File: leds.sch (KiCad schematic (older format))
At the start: 40 parts, among them SW1 SW_PUSH-MX_W_LED, SW10 SW_PUSH-MX_W_LED, SW11 SW_PUSH-MX_W_LED, SW12 SW_PUSH-MX_W_LED, SW13 SW_PUSH-MX_W_LED, SW14 SW_PUSH-MX_W_LED, SW15 SW_PUSH-MX_W_LED, SW16 SW_PUSH-MX_W_LED, SW17 SW_PUSH-MX_W_LED, SW18 SW_PUSH-MX_W_LED, SW19 SW_PUSH-MX_W_LED, SW2 SW_PUSH-MX_W_LED, SW20 SW_PUSH-MX_W_LED, SW3 SW_PUSH-MX_W_LED, SW4 SW_PUSH-MX_W_LED, SW5 SW_PUSH-MX_W_LED, SW6 SW_PUSH-MX_W_LED, SW7 SW_PUSH-MX_W_LED, SW8 SW_PUSH-MX_W_LED, SW9 SW_PUSH-MX_W_LED

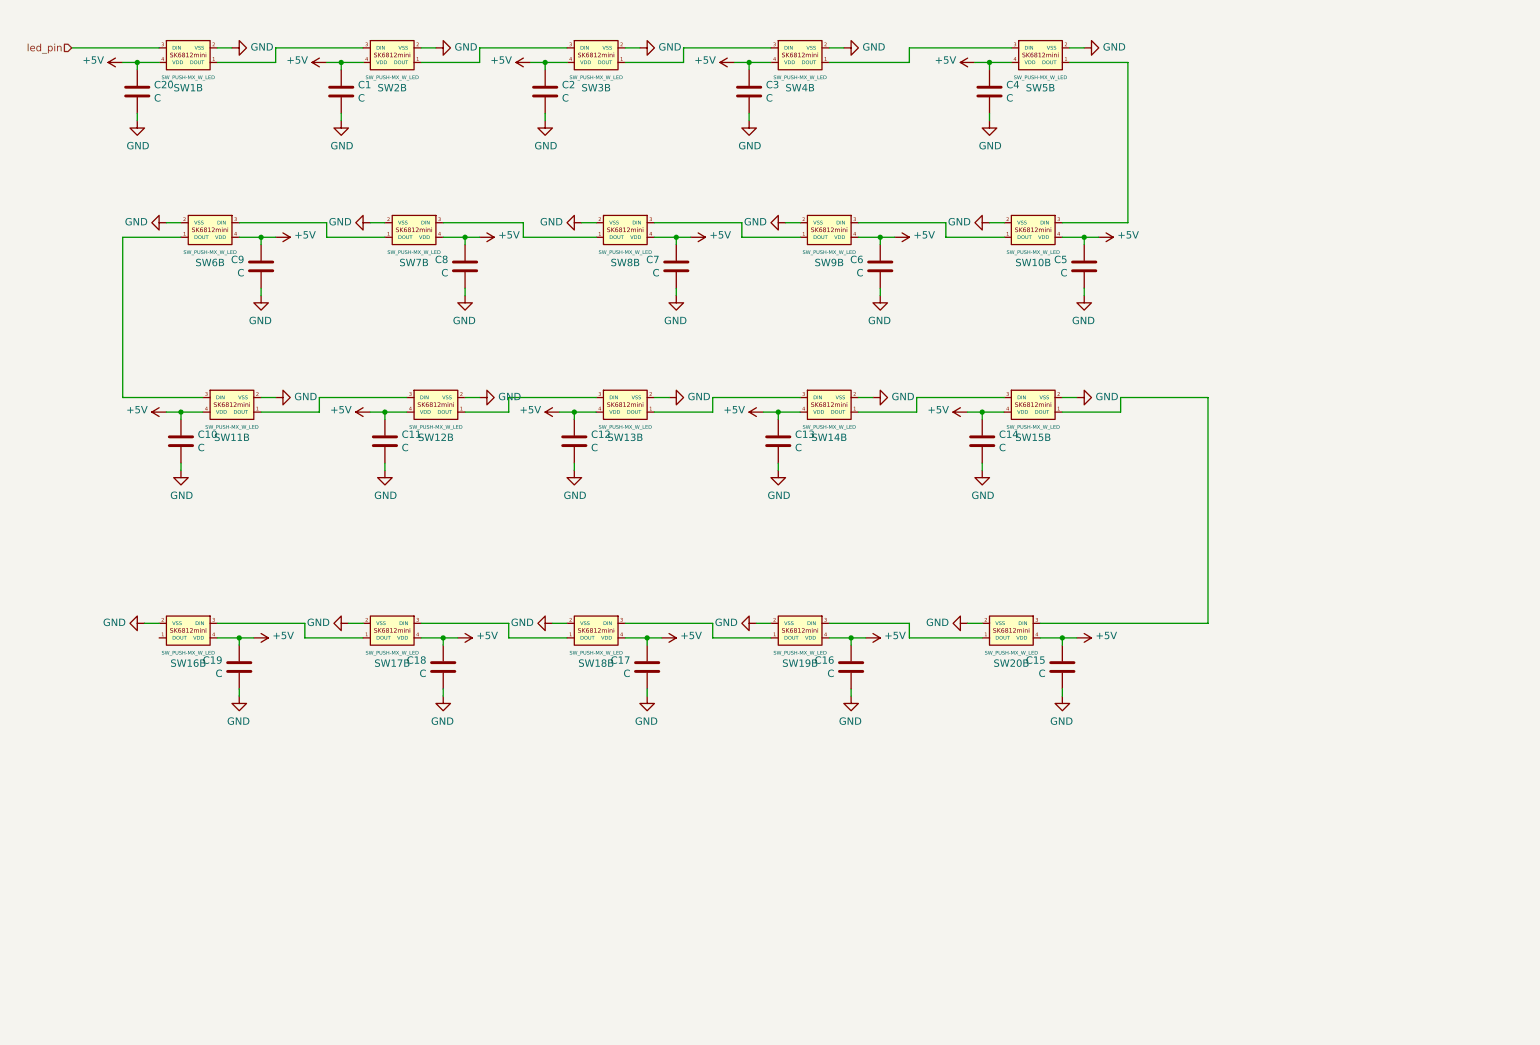
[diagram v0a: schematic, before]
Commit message: kinda done, about to add jumpers for rot. enc.
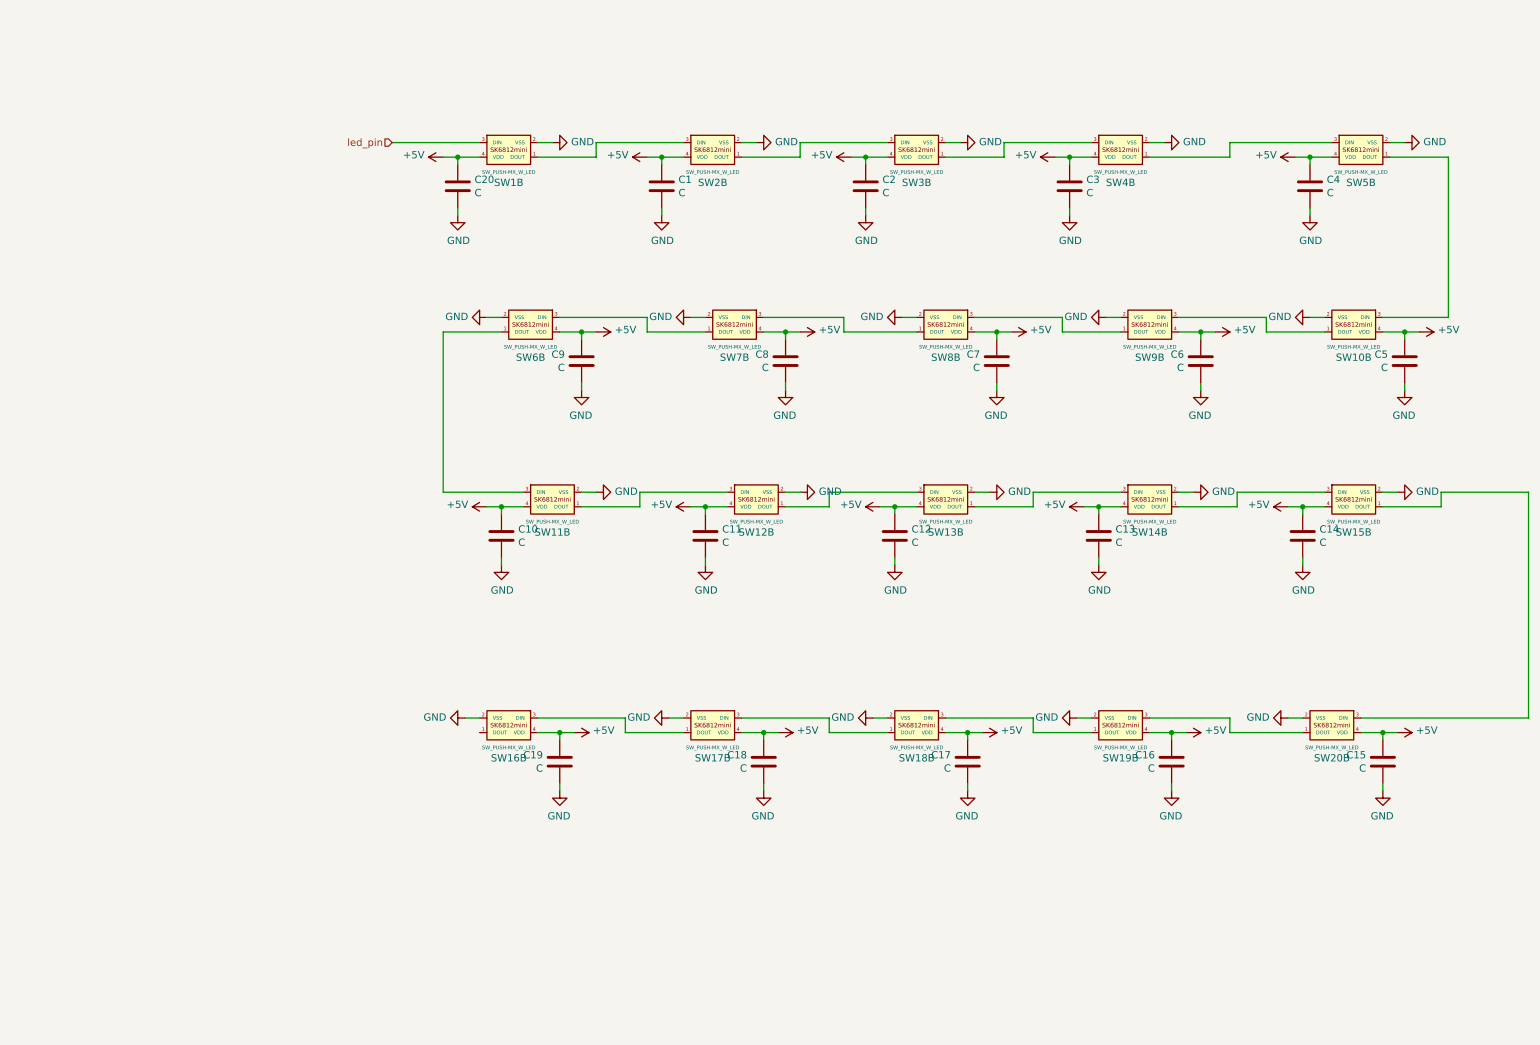
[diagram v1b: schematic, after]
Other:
- moved on the sheet: C1, C10, C11, C12, C13, C14, C15, C16, C17, C18, C19, C2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

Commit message: about to add underglow
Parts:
- added C21, C22, C23, C24: C, Capacitor_SMD:C_0805_2012Metric_Pad1.18x1.45mm_HandSolder, symbol Device:C
- added JP1: Jumper_2_Open, Jumper:SolderJumper-2_P1.3mm_Open_TrianglePad1.0x1.5mm, symbol Jumper:Jumper_2_Open
- added SW23, SW24, SW25, SW26: SW_PUSH-MX_W_LED, sofle RGB:SK6812MINI_and_cherry_oneside_ledflipped, symbol sofle_rgb:SW_PUSH-MX_W_LED
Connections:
- net +5V: now also C21.1, C22.1, C23.1, C24.1, SW23.4 (VDD), SW24.4 (VDD), SW25.4 (VDD), SW26.4 (VDD)
- net GND: now also C21.2, C22.2, C23.2, C24.2, SW23.2 (VSS), SW24.2 (VSS), SW25.2 (VSS), SW26.2 (VSS)
- net led_pin: now also JP1.1 (A)
- net underglow: now reaches SW16.1 (DOUT)
- net underglow: now also JP1.2 (B), SW23.3 (DIN)
- new net: SW23.1 (DOUT), SW24.3 (DIN)
- new net: SW24.1 (DOUT), SW25.3 (DIN)
- new net: SW25.1 (DOUT), SW26.3 (DIN)

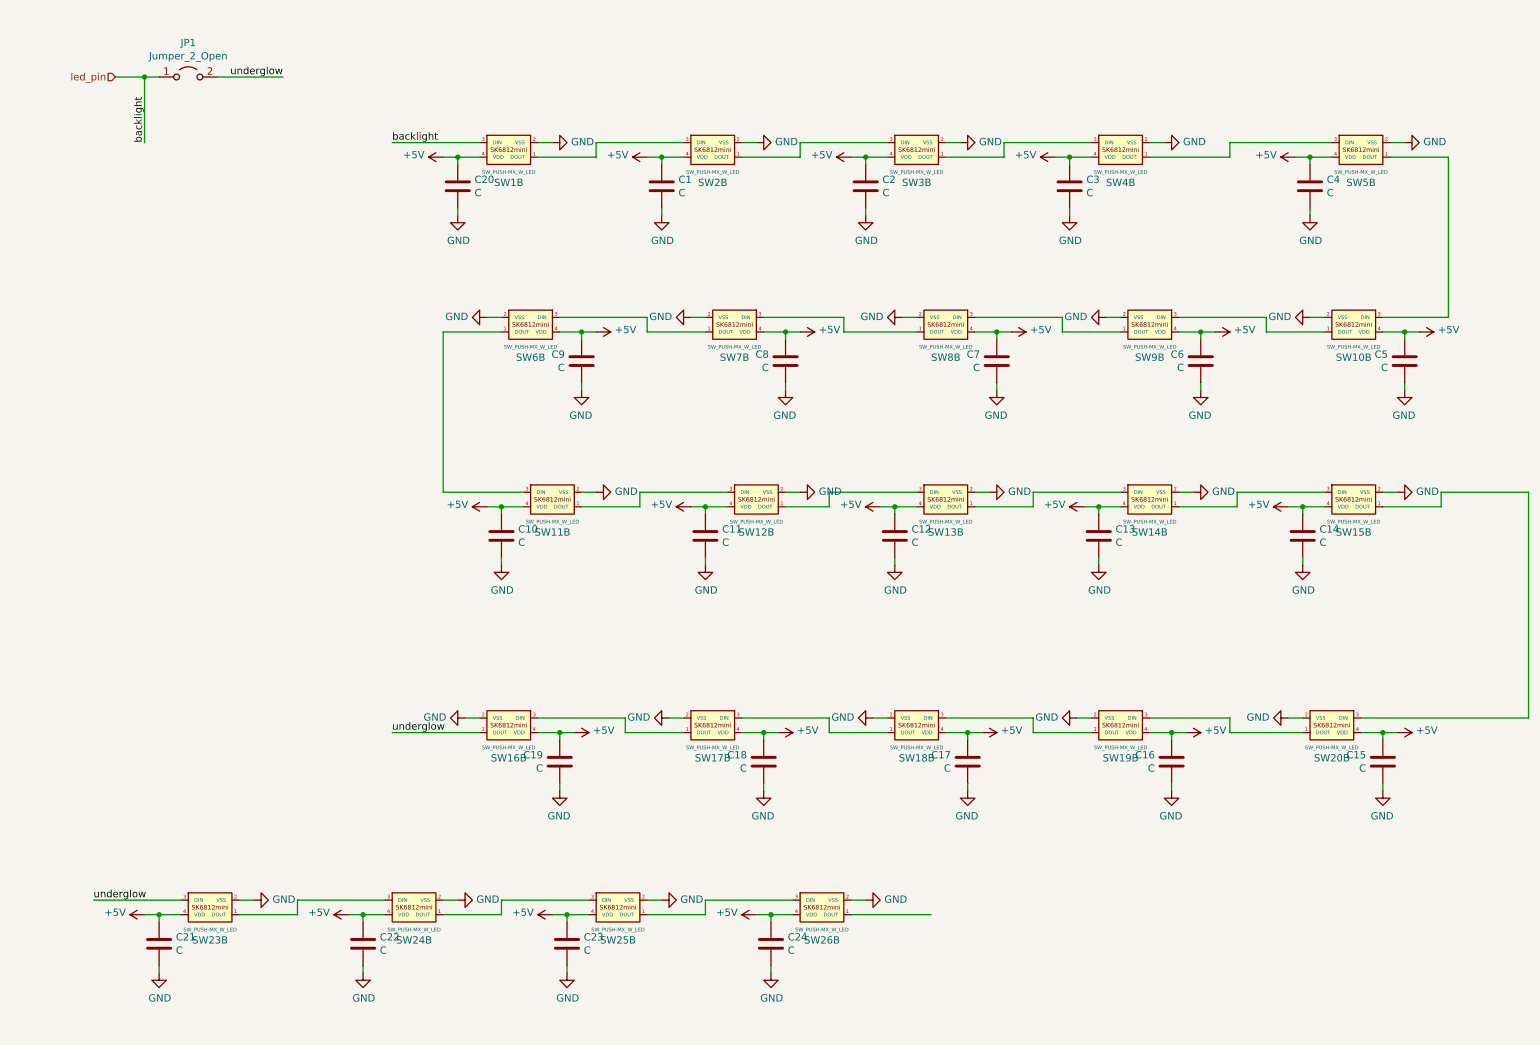
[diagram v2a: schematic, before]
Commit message: added top led and oled display support
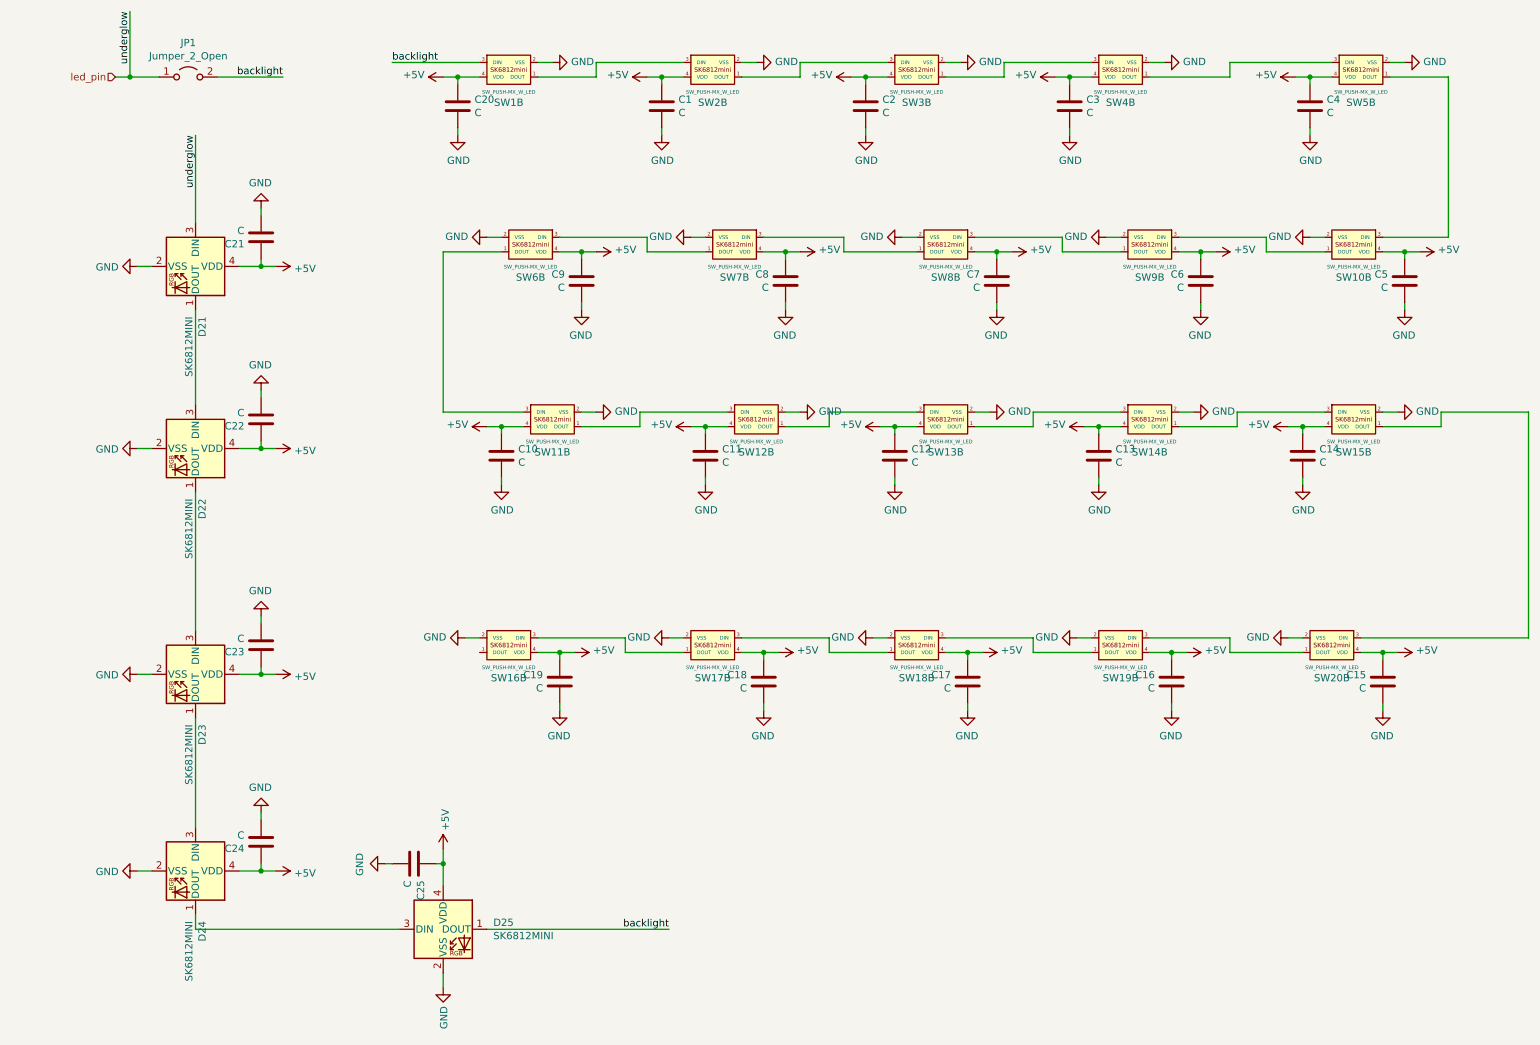
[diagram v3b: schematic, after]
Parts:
- removed SW23, SW24, SW25, SW26: SW_PUSH-MX_W_LED, sofle RGB:SK6812MINI_and_cherry_oneside_ledflipped, symbol sofle_rgb:SW_PUSH-MX_W_LED
- added C25: C, Capacitor_SMD:C_0805_2012Metric_Pad1.18x1.45mm_HandSolder, symbol Device:C
- added D21, D22, D23, D24, D25: SK6812MINI, LED_SMD:LED_SK6812MINI_PLCC4_3.5x3.5mm_P1.75mm, symbol LED:SK6812MINI
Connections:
- net +5V: now also C25.1, D21.4 (VDD), D22.4 (VDD), D23.4 (VDD), D24.4 (VDD), D25.4 (VDD)
- net GND: now also C25.2, D21.2 (VSS), D22.2 (VSS), D23.2 (VSS), D24.2 (VSS), D25.2 (VSS)
- net led_pin: now also D21.3 (DIN); no longer SW1.3 (DIN)
- net underglow: no longer names the net of SW16.1 (DOUT)
- net underglow: no longer JP1.2 (B)
- new net: D21.1 (DOUT), D22.3 (DIN)
- new net: D22.1 (DOUT), D23.3 (DIN)
- new net: D23.1 (DOUT), D24.3 (DIN)
- new net: D24.1 (DOUT), D25.3 (DIN)
- new net backlight: D25.1 (DOUT), JP1.2 (B), SW1.3 (DIN)
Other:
- moved on the sheet: C1, C10, C11, C12, C13, C14, C15, C16, C17, C18, C19, C2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

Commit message: fixed backlight leds; added holes
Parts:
- D21, D22, D23, D24, D25: footprint LED_SMD:LED_SK6812MINI_PLCC4_3.5x3.5mm_P1.75mm -> sofle RGB:LED_SK6812MINI_HS
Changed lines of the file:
@@
 F 0 "D21" H 2144 2496 50  0000 L CNN
 F 1 "SK6812MINI" H 2144 2405 50  0000 L CNN
-F 2 "LED_SMD:LED_SK6812MINI_PLCC4_3.5x3.5mm_P1.75mm" H 1850 2150 50  0001 L TNN
+F 2 "sofle RGB:LED_SK6812MINI_HS" H 1850 2150 50  0001 L TNN
 F 3 "https://cdn-shop.adafruit.com/product-files/2686/SK6812MINI_REV.01-1-2.pdf" H 1900 2075 50  0001 L TNN
 	1    1800 2450
@@
 F 0 "D22" H 2144 3746 50  0000 L CNN
 F 1 "SK6812MINI" H 2144 3655 50  0000 L CNN
-F 2 "LED_SMD:LED_SK6812MINI_PLCC4_3.5x3.5mm_P1.75mm" H 1850 3400 50  0001 L TNN
+F 2 "sofle RGB:LED_SK6812MINI_HS" H 1850 3400 50  0001 L TNN
 F 3 "https://cdn-shop.adafruit.com/product-files/2686/SK6812MINI_REV.01-1-2.pdf" H 1900 3325 50  0001 L TNN
 	1    1800 3700
@@
 F 0 "D23" H 2144 5296 50  0000 L CNN
 F 1 "SK6812MINI" H 2144 5205 50  0000 L CNN
-F 2 "LED_SMD:LED_SK6812MINI_PLCC4_3.5x3.5mm_P1.75mm" H 1850 4950 50  0001 L TNN
+F 2 "sofle RGB:LED_SK6812MINI_HS" H 1850 4950 50  0001 L TNN
 F 3 "https://cdn-shop.adafruit.com/product-files/2686/SK6812MINI_REV.01-1-2.pdf" H 1900 4875 50  0001 L TNN
 	1    1800 5250
@@
 F 0 "D24" H 2144 6646 50  0000 L CNN
 F 1 "SK6812MINI" H 2144 6555 50  0000 L CNN
-F 2 "LED_SMD:LED_SK6812MINI_PLCC4_3.5x3.5mm_P1.75mm" H 1850 6300 50  0001 L TNN
+F 2 "sofle RGB:LED_SK6812MINI_HS" H 1850 6300 50  0001 L TNN
 F 3 "https://cdn-shop.adafruit.com/product-files/2686/SK6812MINI_REV.01-1-2.pdf" H 1900 6225 50  0001 L TNN
 	1    1800 6600
@@
 F 0 "D25" H 3844 7046 50  0000 L CNN
 F 1 "SK6812MINI" H 3844 6955 50  0000 L CNN
-F 2 "LED_SMD:LED_SK6812MINI_PLCC4_3.5x3.5mm_P1.75mm" H 3550 6700 50  0001 L TNN
+F 2 "sofle RGB:LED_SK6812MINI_HS" H 3550 6700 50  0001 L TNN
 F 3 "https://cdn-shop.adafruit.com/product-files/2686/SK6812MINI_REV.01-1-2.pdf" H 3600 6625 50  0001 L TNN
 	1    3500 7000
